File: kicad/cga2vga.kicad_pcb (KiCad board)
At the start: 2 copper layers, 173.2 x 31.7 mm, 18 parts, among them J1 Conn_02x24_Counter_Clockwise, J2 CGA, J3 VGA, J4 5V, U1 MCP1700-3302E_TO92, U2 SN74LVC245A, U3 SN74LVC245A

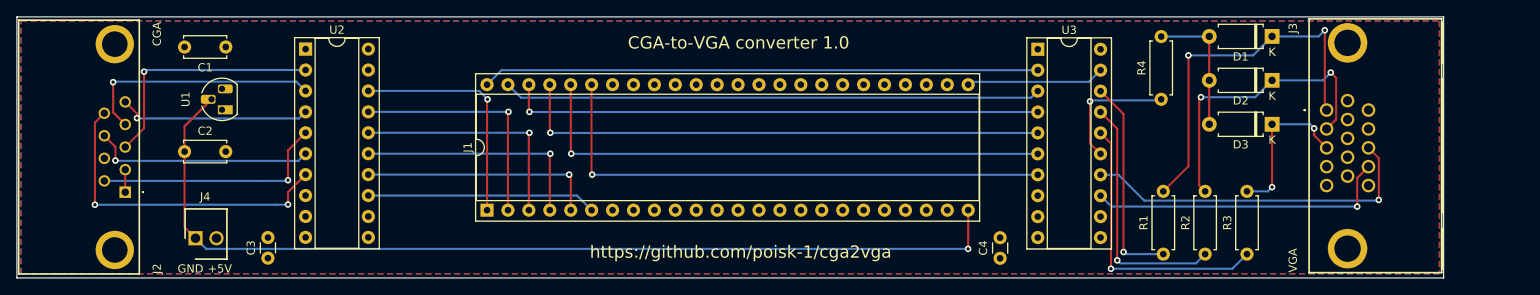
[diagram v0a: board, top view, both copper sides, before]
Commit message: Fix power connector marking
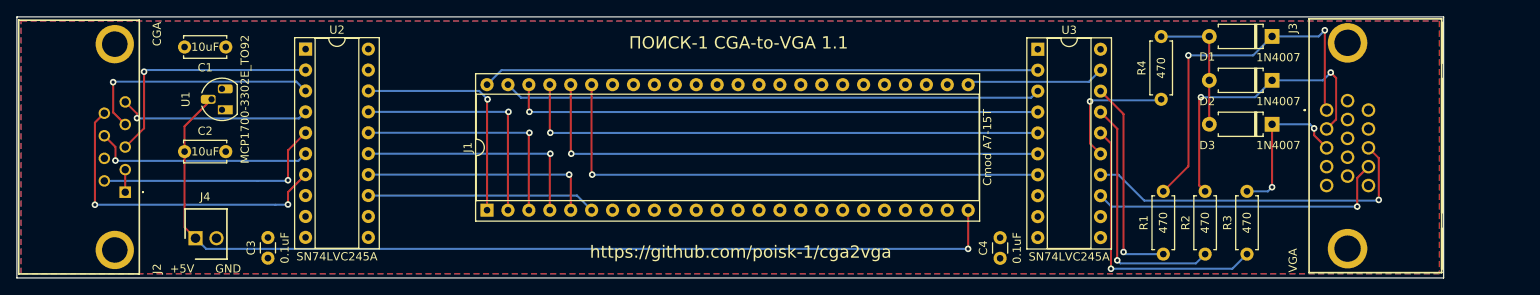
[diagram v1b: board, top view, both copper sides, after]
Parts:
- J1: value Conn_02x24_Counter_Clockwise -> Cmod A7-15T
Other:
- board text added: "ПОИСК-1 CGA-to-VGA 1.1"
- board text removed: "CGA-to-VGA converter 1.0"
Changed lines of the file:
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@@
   (net 79 "unconnected-(U3-Pad9)")
   (footprint "Diode_THT:D_A-405_P7.62mm_Horizontal" (layer "F.Cu")
-    (at 201.168 91.679 180)
+    (at 201.168 91.678989 180)
     (descr "Diode, A-405 series, Axial, Horizontal, pin pitch=7.62mm, , length*diameter=5.2*2.7mm^2, , http://www.diodes.com/_files/packages/A-405.pdf")
     (tags "Diode A-405 series Axial Horizontal pin pitch 7.62mm  length 5.2mm diameter 2.7mm")
@@
     (property "Sheetname" "")
     (attr through_hole)
-    (fp_text reference "D3" (at 3.81 -2.47) (layer "F.SilkS")
-      (effects (font (size 1 1) (thickness 0.15)))
-    )
-    (fp_text value "1N4007" (at 3.81 2.47) (layer "F.Fab")
-      (effects (font (size 1 1) (thickness 0.15)))
-    )
-    (fp_text user "K" (at 0 -1.9) (layer "F.SilkS")
+    (fp_text reference "D3" (at 7.874 -2.555011) (layer "F.SilkS")
+      (effects (font (size 1 1) (thickness 0.15)))
+    )
+    (fp_text value "1N4007" (at -0.762 -2.555011) (layer "F.SilkS")
+      (effects (font (size 1 1) (thickness 0.15)))
+    )
+    (fp_text user "K" (at 0 -1.9) (layer "F.Fab")
       (effects (font (size 1 1) (thickness 0.15)))
     )
@@
       (effects (font (size 1 1) (thickness 0.15)))
     )
-    (fp_text value "470" (at 3.81 2.37 90) (layer "F.Fab")
+    (fp_text value "470" (at 3.81 0 90) (layer "F.SilkS")
       (effects (font (size 1 1) (thickness 0.15)))
     )
@@
       (effects (font (size 1 1) (thickness 0.15)))
     )
-    (fp_text value "470" (at 3.81 2.37 90) (layer "F.Fab")
+    (fp_text value "470" (at 3.81 0 90) (layer "F.SilkS")
       (effects (font (size 1 1) (thickness 0.15)))
     )
@@
       (effects (font (size 1 1) (thickness 0.15)))
     )
-    (fp_text value "470" (at 3.81 2.37 90) (layer "F.Fab")
+    (fp_text value "470" (at 3.81 0 90) (layer "F.SilkS")
       (effects (font (size 1 1) (thickness 0.15)))
     )
@@
   )
   (footprint "Package_DIP:DIP-48_W15.24mm_Socket" (layer "F.Cu")
-    (at 105.852 102.108 90)
+    (at 105.852011 102.108 90)
     (descr "48-lead though-hole mounted DIP package, row spacing 15.24 mm (600 mils), Socket")
     (tags "THT DIP DIL PDIP 2.54mm 15.24mm 600mil Socket")
@@
       (effects (font (size 1 1) (thickness 0.15)))
     )
-    (fp_text value "Conn_02x24_Counter_Clockwise" (at 7.62 60.75 90) (layer "F.Fab")
+    (fp_text value "Cmod A7-15T" (at 7.62 60.75 90) (layer "F.SilkS")
       (effects (font (size 1 1) (thickness 0.15)))
     )
@@
   )
   (footprint "Diode_THT:D_A-405_P7.62mm_Horizontal" (layer "F.Cu")
-    (at 201.168 86.345 180)
+    (at 201.168 86.344989 180)
     (descr "Diode, A-405 series, Axial, Horizontal, pin pitch=7.62mm, , length*diameter=5.2*2.7mm^2, , http://www.diodes.com/_files/packages/A-405.pdf")
     (tags "Diode A-405 series Axial Horizontal pin pitch 7.62mm  length 5.2mm diameter 2.7mm")
@@
     (property "Sheetname" "")
     (attr through_hole)
-    (fp_text reference "D2" (at 3.81 -2.47) (layer "F.SilkS")
-      (effects (font (size 1 1) (thickness 0.15)))
-    )
-    (fp_text value "1N4007" (at 3.81 2.47) (layer "F.Fab")
-      (effects (font (size 1 1) (thickness 0.15)))
-    )
-    (fp_text user "K" (at 0 -1.9) (layer "F.SilkS")
+    (fp_text reference "D2" (at 7.874 -2.555011) (layer "F.SilkS")
+      (effects (font (size 1 1) (thickness 0.15)))
+    )
+    (fp_text value "1N4007" (at -0.762 -2.555011) (layer "F.SilkS")
+      (effects (font (size 1 1) (thickness 0.15)))
+    )
+    (fp_text user "K" (at 0 -1.9) (layer "F.Fab")
       (effects (font (size 1 1) (thickness 0.15)))
     )
@@
       (effects (font (size 1 1) (thickness 0.15)))
     )
-    (fp_text value "SN74LVC245A" (at 3.81 25.19) (layer "F.Fab")
+    (fp_text value "SN74LVC245A" (at 3.81 25.19) (layer "F.SilkS")
       (effects (font (size 1 1) (thickness 0.15)))
     )
@@
       (effects (font (size 1 1) (thickness 0.15)))
     )
-    (fp_text value "470" (at 3.81 2.37 90) (layer "F.Fab")
+    (fp_text value "470" (at 3.81 0 90) (layer "F.SilkS")
       (effects (font (size 1 1) (thickness 0.15)))
     )
@@
   )
   (footprint "Diode_THT:D_A-405_P7.62mm_Horizontal" (layer "F.Cu")
-    (at 201.168 81.011 180)
+    (at 201.168 81.010989 180)
     (descr "Diode, A-405 series, Axial, Horizontal, pin pitch=7.62mm, , length*diameter=5.2*2.7mm^2, , http://www.diodes.com/_files/packages/A-405.pdf")
     (tags "Diode A-405 series Axial Horizontal pin pitch 7.62mm  length 5.2mm diameter 2.7mm")
@@
     (property "Sheetname" "")
     (attr through_hole)
-    (fp_text reference "D1" (at 3.81 -2.47) (layer "F.SilkS")
-      (effects (font (size 1 1) (thickness 0.15)))
-    )
-    (fp_text value "1N4007" (at 3.81 2.47) (layer "F.Fab")
-      (effects (font (size 1 1) (thickness 0.15)))
-    )
-    (fp_text user "K" (at 0 -1.9) (layer "F.SilkS")
+    (fp_text reference "D1" (at 7.874 -2.47) (layer "F.SilkS")
+      (effects (font (size 1 1) (thickness 0.15)))
+    )
+    (fp_text value "1N4007" (at -0.762 -2.555011) (layer "F.SilkS")
+      (effects (font (size 1 1) (thickness 0.15)))
+    )
+    (fp_text user "K" (at 0 -1.9) (layer "F.Fab")
       (effects (font (size 1 1) (thickness 0.15)))
     )
@@
   )
   (footprint "Package_DIP:DIP-20_W7.62mm_Socket" (layer "F.Cu")
-    (at 172.72 82.57)
+    (at 172.72 82.56999)
     (descr "20-lead though-hole mounted DIP package, row spacing 7.62 mm (300 mils), Socket")
     (tags "THT DIP DIL PDIP 2.54mm 7.62mm 300mil Socket")
@@
       (effects (font (size 1 1) (thickness 0.15)))
     )
-    (fp_text value "SN74LVC245A" (at 3.81 25.19) (layer "F.Fab")
+    (fp_text value "SN74LVC245A" (at 3.81 25.19) (layer "F.SilkS")
       (effects (font (size 1 1) (thickness 0.15)))
     )
@@
   )
   (footprint "Capacitor_THT:C_Disc_D5.0mm_W2.5mm_P5.00mm" (layer "F.Cu")
-    (at 69.128 94.996)
+    (at 69.128005 94.996)
     (descr "C, Disc series, Radial, pin pitch=5.00mm, , diameter*width=5*2.5mm^2, Capacitor, http://cdn-reichelt.de/documents/datenblatt/B300/DS_KERKO_TC.pdf")
     (tags "C Disc series Radial pin pitch 5.00mm  diameter 5mm width 2.5mm Capacitor")
@@
       (effects (font (size 1 1) (thickness 0.15)))
     )
-    (fp_text value "10uF" (at 2.5 2.5) (layer "F.Fab")
+    (fp_text value "10uF" (at 2.499995 0) (layer "F.SilkS")
       (effects (font (size 1 1) (thickness 0.15)))
     )
@@
   )
   (footprint "Package_TO_SOT_THT:TO-92_HandSolder" (layer "F.Cu")
-    (at 73.672 89.916 90)
+    (at 73.671989 89.916 90)
     (descr "TO-92 leads molded, narrow, drill 0.75mm, handsoldering variant with enlarged pads (see NXP sot054_po.pdf)")
     (tags "to-92 sc-43 sc-43a sot54 PA33 transistor")
@@
       (effects (font (size 1 1) (thickness 0.15)))
     )
-    (fp_text value "MCP1700-3302E_TO92" (at 1.27 2.79 90) (layer "F.Fab")
+    (fp_text value "MCP1700-3302E_TO92" (at 1.27 2.79 90) (layer "F.SilkS")
       (effects (font (size 1 1) (thickness 0.15)))
     )
@@
   )
   (footprint "Capacitor_THT:C_Disc_D5.0mm_W2.5mm_P5.00mm" (layer "F.Cu")
-    (at 74.128 82.296 180)
+    (at 74.127995 82.296 180)
     (descr "C, Disc series, Radial, pin pitch=5.00mm, , diameter*width=5*2.5mm^2, Capacitor, http://cdn-reichelt.de/documents/datenblatt/B300/DS_KERKO_TC.pdf")
     (tags "C Disc series Radial pin pitch 5.00mm  diameter 5mm width 2.5mm Capacitor")
@@
       (effects (font (size 1 1) (thickness 0.15)))
     )
-    (fp_text value "10uF" (at 2.5 2.5) (layer "F.Fab")
+    (fp_text value "10uF" (at 2.5 0) (layer "F.SilkS")
       (effects (font (size 1 1) (thickness 0.15)))
     )
@@
       (effects (font (size 1 1) (thickness 0.15)))
     )
-    (fp_text value "0.1uF" (at 1.25 2.05 90) (layer "F.Fab")
+    (fp_text value "0.1uF" (at 1.25 2.05 90) (layer "F.SilkS")
       (effects (font (size 1 1) (thickness 0.15)))
     )
@@
   )
   (footprint "Capacitor_THT:C_Disc_D3.0mm_W1.6mm_P2.50mm" (layer "F.Cu")
-    (at 79.248 107.93 90)
+    (at 79.248 107.93001 90)
     (descr "C, Disc series, Radial, pin pitch=2.50mm, , diameter*width=3.0*1.6mm^2, Capacitor, http://www.vishay.com/docs/45233/krseries.pdf")
     (tags "C Disc series Radial pin pitch 2.50mm  diameter 3.0mm width 1.6mm Capacitor")
@@
       (effects (font (size 1 1) (thickness 0.15)))
     )
-    (fp_text value "0.1uF" (at 1.25 2.05 90) (layer "F.Fab")
+    (fp_text value "0.1uF" (at 1.25 2.05 90) (layer "F.SilkS")
       (effects (font (size 1 1) (thickness 0.15)))
     )
@@
   (gr_line (start 48.768 78.6384) (end 221.996 78.6384) (layer "Edge.Cuts") (width 0.1))
   (gr_line (start 221.996 78.74) (end 221.996 78.6384) (layer "Edge.Cuts") (width 0.1))
-  (gr_text "CGA-to-VGA converter 1.0" (at 136.398 81.788) (layer "F.SilkS")
+  (gr_text "ПОИСК-1 CGA-to-VGA 1.1" (at 136.398 81.788) (layer "F.SilkS")
     (effects (font (size 1.5 1.5) (thickness 0.3)))
   )
-  (gr_text "GND" (at 69.85 109.22) (layer "F.SilkS")
+  (gr_text "GND" (at 74.422 109.22) (layer "F.SilkS")
     (effects (font (size 1 1) (thickness 0.14986)))
   )
-  (gr_text "+5V" (at 73.406 109.22) (layer "F.SilkS")
+  (gr_text "+5V" (at 68.834 109.22) (layer "F.SilkS")
     (effects (font (size 1 1) (thickness 0.14986)))
   )

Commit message: Update PCB
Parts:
- added R5: 680, Resistor_THT:R_Axial_DIN0207_L6.3mm_D2.5mm_P7.62mm_Horizontal, F.Cu at (193.0, 88.6)
- added R6: 680, Resistor_THT:R_Axial_DIN0207_L6.3mm_D2.5mm_P7.62mm_Horizontal, F.Cu at (198.1, 88.6)
- R4: value 470 -> 680
- moved J3 9.68 mm to (217.5, 89.9)
- moved D1 9.60 mm to (210.8, 81.0)
- moved D2 9.60 mm to (210.8, 86.3)
- moved D3 9.60 mm to (210.8, 91.6)
- moved R4 0.25 mm to (188.0, 88.6)
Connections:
- net /GEN_RGBI_0 renamed /GEN_RGB0_0
- net /GEN_RGBI_1 renamed /GEN_RGB0_1
- net /GEN_RGBI_2 renamed /GEN_RGB0_2
- net /GEN_RGBI_3 renamed /GEN_RGB1_0
- D2 pad 2: Net-(D1-Pad2) -> Net-(D2-Pad2)
- D3 pad 2: Net-(D1-Pad2) -> Net-(D3-Pad2)
- J1 pad 41: unconnected-(J1-Pad41) -> /GEN_SYNC_1
- J1 pad 42: unconnected-(J1-Pad42) -> /GEN_SYNC_0
- J1 pad 43: /GEN_SYNC_1 -> /GEN_RGB1_2
- J1 pad 44: /GEN_SYNC_0 -> /GEN_RGB1_1
- U2 pad 8: unconnected-(U2-Pad8) -> GND
- U2 pad 9: unconnected-(U2-Pad9) -> GND
- U3 pad 11: unconnected-(U3-Pad11) -> VGA_VSYNC
- U3 pad 12: unconnected-(U3-Pad12) -> VGA_HSYNC
- U3 pad 13: VGA_VSYNC -> Net-(R6-Pad1)
- U3 pad 14: VGA_HSYNC -> Net-(R5-Pad1)
- U3 pad 6: /GEN_SYNC_0 -> /GEN_RGB1_1
- U3 pad 7: /GEN_SYNC_1 -> /GEN_RGB1_2
- U3 pad 8: unconnected-(U3-Pad8) -> /GEN_SYNC_0
- U3 pad 9: unconnected-(U3-Pad9) -> /GEN_SYNC_1
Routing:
- net /GEN_RGB1_1: track 0.00 -> 65.1 mm, vias 0 -> 1
- net /GEN_RGB1_2: track 0.00 -> 65.1 mm, vias 0 -> 1
- net Net-(R6-Pad1): track 0.00 -> 29.6 mm, vias 0 -> 1
- net Net-(R5-Pad1): track 0.00 -> 21.1 mm, vias 0 -> 1
- net Net-(D2-Pad2): track 0.00 -> 15.4 mm, vias 0 -> 1
- net Net-(D3-Pad2): track 0.00 -> 15.0 mm, vias 0 -> 1
- net VGA_VSYNC: track 37.1 -> 49.4 mm
- net VGA_HSYNC: track 42.0 -> 52.2 mm
- net VGA_B: track 19.2 -> 28.7 mm, vias 2 -> 1
- net VGA_R: track 45.4 -> 50.3 mm, vias 2 -> 1
- net /GEN_SYNC_1: track 65.1 -> 68.0 mm
- net VGA_G: track 36.4 -> 38.9 mm, vias 2 -> 1
- net Net-(R4-Pad1): track 15.6 -> 14.2 mm
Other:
- board size 173.2 x 31.7 mm -> 182.9 x 31.7 mm
- board text added: "ПОИСК-1 CGA-to-VGA 1.2"
- board text removed: "ПОИСК-1 CGA-to-VGA 1.1"
